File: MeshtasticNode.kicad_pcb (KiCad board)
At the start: 4 copper layers, 71.3 x 72.8 mm, 38 parts, among them J1 Conn_01x02_Socket, J2 Conn_01x02_Socket, J3 Conn_01x04_Socket, J4 Conn_01x03_Pin, J5 Conn_01x03_Pin, J6 Conn_01x03_Pin, J8 Conn_01x03_Pin, U1 BQ24074, U2 HT-CT62, U8 XC6206PxxxMR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

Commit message: Increase maximum current from 500mA to 2A
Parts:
- R1: value 2k -> 500
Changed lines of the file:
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@@
 			)
 		)
-		(property "Value" "2k"
+		(property "Value" "500"
 			(at 0 1.65 90)
 			(layer "F.Fab")

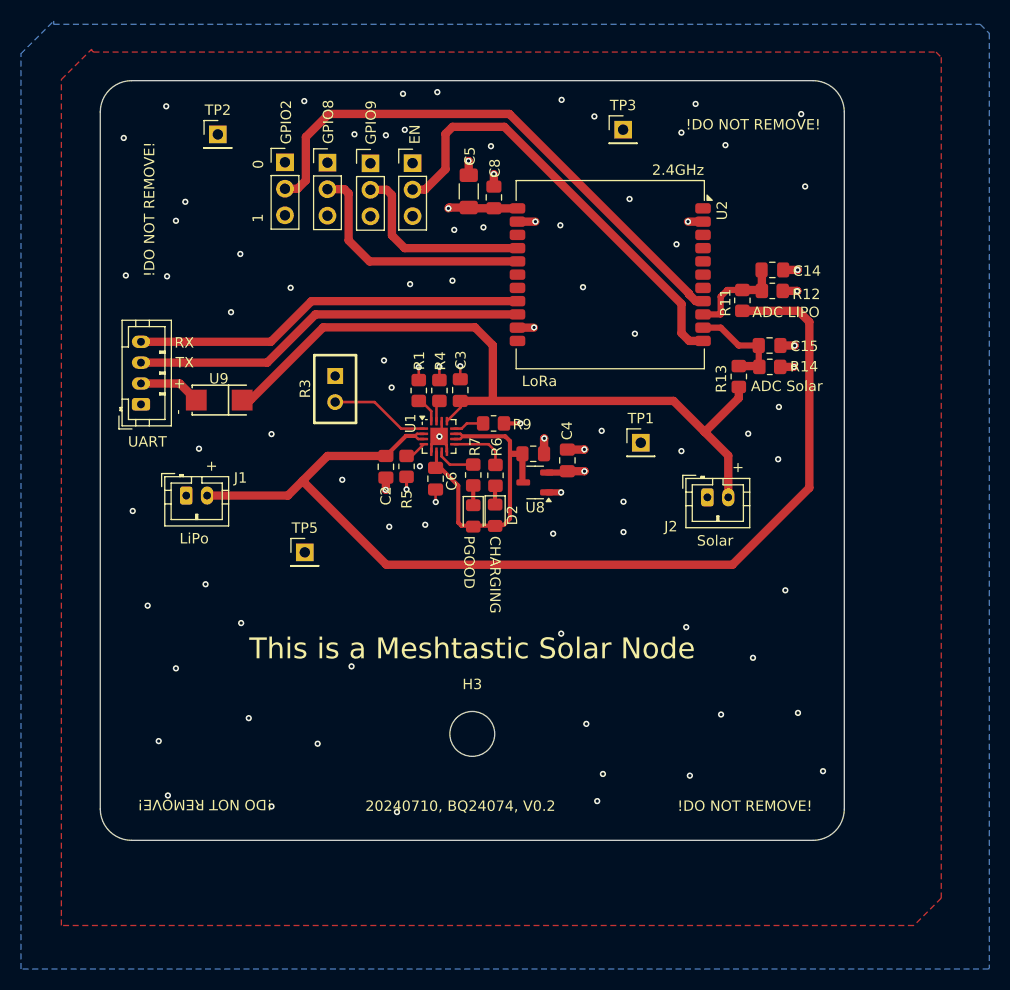
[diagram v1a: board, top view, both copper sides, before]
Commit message: pcb: Make EN1 and EN2 selectable. Fixes awful bug.
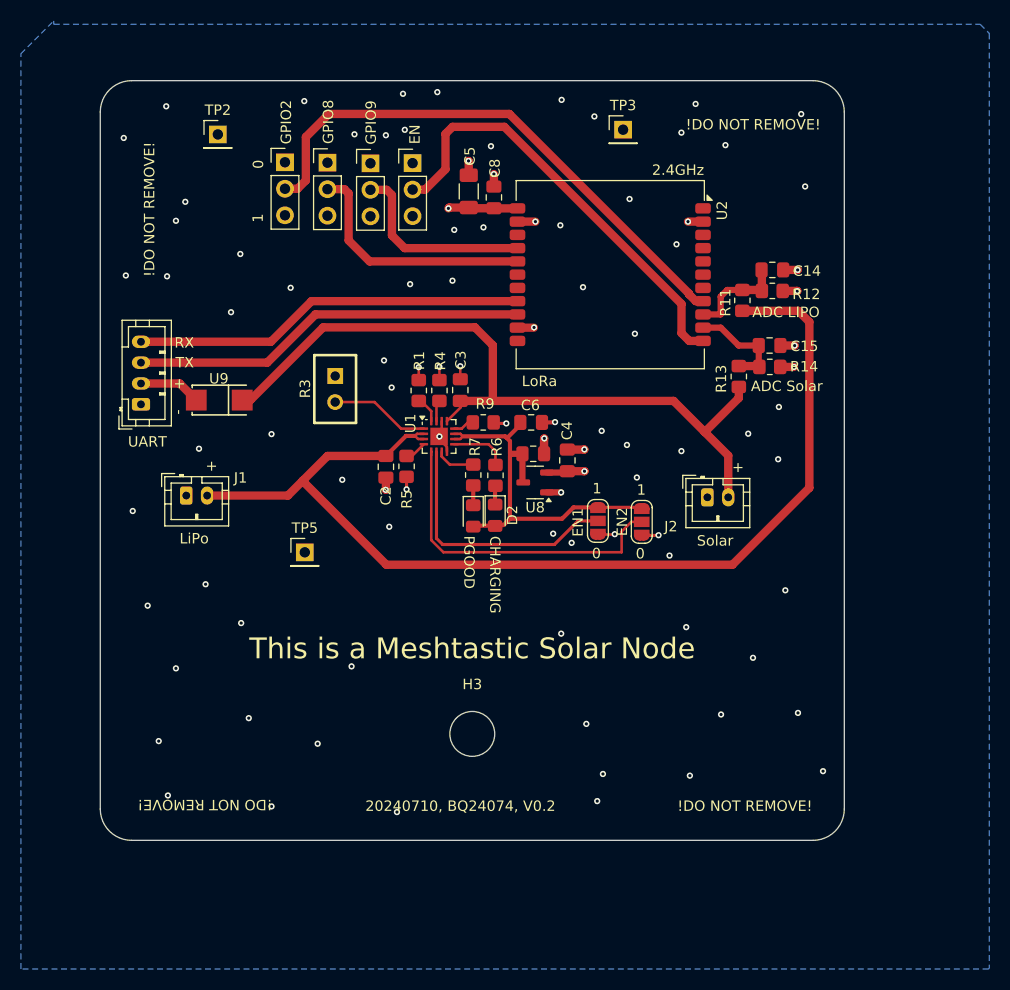
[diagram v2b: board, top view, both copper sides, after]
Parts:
- removed TP1: TestPoint, Connector_PinHeader_2.54mm:PinHeader_1x01_P2.54mm_Vertical
- added JP1: SolderJumper_3_Open, Jumper:SolderJumper-3_P1.3mm_Open_RoundedPad1.0x1.5mm_NumberLabels, F.Cu at (230.8, 71.5)
- added JP2: SolderJumper_3_Open, Jumper:SolderJumper-3_P1.3mm_Open_RoundedPad1.0x1.5mm_NumberLabels, F.Cu at (235.0, 71.6)
- moved C6 10.6 mm to (224.4, 62.0), turned to 180 degrees
- moved R9 0.99 mm to (219.8, 62.0)
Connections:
- U1 pad 5: GND -> /EN2
- U1 pad 6: /OUT -> /EN1
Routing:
- net /EN2: track 0.00 -> 31.5 mm
- net /EN1: track 0.00 -> 25.0 mm
- net /OUT: track 30.6 -> 36.7 mm
- net GND: track 29.2 -> 31.9 mm, vias 91 -> 93
- net Net-(U1-ILIM): track 2.97 -> 2.02 mm
- removed copper zone on F.Cu, net GND
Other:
- board text added: "EN1"
- board text added: "EN2"

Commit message: pcb: prepare for v0.3
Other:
- board text added: "20240710, BQ24074, V0.3"
- board text removed: "20240710, BQ24074, V0.2"
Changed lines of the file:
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@@
 		(tags "capacitor handsolder")
 		(property "Reference" "C6"
-			(at 0.07 1.64 360)
+			(at 0.07 1.64 0)
 			(layer "F.SilkS")
 			(effects
@@
 		)
 		(property "Value" "4.7uF"
-			(at 0 1.68 360)
+			(at 0 1.68 0)
 			(layer "F.Fab")
 			(hide yes)
@@
 		)
 		(fp_text user "${REFERENCE}"
-			(at 0 0 360)
+			(at 0 0 0)
 			(layer "F.Fab")
 			(effects
@@
 		)
 	)
-	(gr_text "20240710, BQ24074, V0.2"
+	(gr_text "20240710, BQ24074, V0.3"
 		(at 208.5 99.4 0)
 		(layer "F.SilkS")
